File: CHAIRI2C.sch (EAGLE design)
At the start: 20 parts, among them IC1 DS3502, IC2 DS3502, X1 OUTPUT

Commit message: Changed VREF on digital pots for v1.0 release
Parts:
- added U$8, U$9: FIDUCIAL1X2.5, SuperHouse-Symbols:FIDUCIAL1X2.5
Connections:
- net 12V: now also IC1.VBIAS, IC2.VBIAS
- net N$2: no longer IC1.VBIAS
- net N$3: no longer IC2.VBIAS
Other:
- note added: "(C)2020 SuperHouse Automation: www.superhouse.tv"
- note added: "Direction Control (X Axis)"
- note added: "Power Indicators"
- note added: "Speed Control (Y Axis)"
- note removed: "(C)2018-2020 SuperHouse Automation: www.superhouse.tv"
- note removed: "Direction Control"
- note removed: "Power / Status"
- note removed: "Speed Control"
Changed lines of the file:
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@@
 <part name="U$2" library="SuperHouse-Jumpers" library_urn="urn:adsk.eagle:library:12190622" deviceset="SJC" device="-NORMAL" package3d_urn="urn:adsk.eagle:package:7066342/1" value="PU"/>
 <part name="U$3" library="SuperHouse-Jumpers" library_urn="urn:adsk.eagle:library:12190622" deviceset="SJC" device="-NORMAL" package3d_urn="urn:adsk.eagle:package:7066342/1" value="PU"/>
+<part name="U$8" library="SuperHouse-Symbols" library_urn="urn:adsk.eagle:library:13228893" deviceset="FIDUCIAL" device="1X2.5" package3d_urn="urn:adsk.eagle:package:13228898/1"/>
+<part name="U$9" library="SuperHouse-Symbols" library_urn="urn:adsk.eagle:library:13228893" deviceset="FIDUCIAL" device="1X2.5" package3d_urn="urn:adsk.eagle:package:13228898/1"/>
 </parts>
 <sheets>
@@
 <text x="172.72" y="14.478" size="1.778" layer="94">V1.0 (2020-05-05)</text>
 <text x="142.24" y="14.478" size="1.778" layer="94">SKU: CHAIRI2C</text>
-<text x="141.986" y="9.398" size="1.778" layer="94">(C)2018-2020 SuperHouse Automation: www.superhouse.tv</text>
+<text x="141.986" y="9.398" size="1.778" layer="94">(C)2020 SuperHouse Automation: www.superhouse.tv</text>
 <text x="141.986" y="6.35" size="1.778" layer="94">Licensed under the TAPR Open Hardware License: www.tapr.org/ohl</text>
 <text x="202.946" y="14.478" size="1.778" layer="94">www.superhouse.tv/chairi2c</text>
-<text x="66.04" y="50.8" size="2.54" layer="94" ratio="12">Power / Status</text>
+<text x="66.04" y="50.8" size="2.54" layer="94" ratio="12">Power Indicators</text>
 <frame x1="139.7" y1="12.7" x2="243.84" y2="25.4" columns="0" rows="0" layer="94" border-left="no" border-top="no" border-right="no" border-bottom="no"/>
 <frame x1="139.7" y1="12.7" x2="170.18" y2="17.78" columns="8" rows="5" layer="94"/>
 <frame x1="170.18" y1="12.7" x2="200.66" y2="17.78" columns="8" rows="5" layer="94"/>
 <frame x1="139.7" y1="5.08" x2="243.84" y2="17.78" columns="0" rows="0" layer="94" border-left="no" border-top="no" border-right="no" border-bottom="no"/>
-<text x="71.12" y="106.68" size="2.54" layer="94" ratio="12">Direction Control</text>
-<text x="71.12" y="162.56" size="2.54" layer="94" ratio="12">Speed Control</text>
+<text x="71.12" y="106.68" size="2.54" layer="94" ratio="12">Direction Control (X Axis)</text>
+<text x="71.12" y="162.56" size="2.54" layer="94" ratio="12">Speed Control (Y Axis)</text>
 <text x="167.64" y="139.7" size="2.54" layer="94" ratio="12">Chair Interface</text>
 <wire x1="129.54" y1="119.38" x2="129.54" y2="167.64" width="0.3048" layer="97" style="longdash"/>
@@
 <attribute name="VALUE" x="49.53" y="124.46" size="1.778" layer="96" rot="R90"/>
 </instance>
+<instance part="U$8" gate="G$1" x="238.76" y="27.94" smashed="yes"/>
+<instance part="U$9" gate="G$1" x="233.68" y="27.94" smashed="yes"/>
 </instances>
 <busses>
@@
 <segment>
 <pinref part="IC1" gate="G$1" pin="RW"/>
-<wire x1="109.22" y1="142.24" x2="149.86" y2="142.24" width="0.1524" layer="91"/>
+<wire x1="109.22" y1="142.24" x2="137.16" y2="142.24" width="0.1524" layer="91"/>
 <pinref part="X1" gate="G$1" pin="1"/>
-<label x="149.86" y="116.84" size="1.27" layer="95" rot="R180" xref="yes"/>
-<wire x1="149.86" y1="116.84" x2="198.12" y2="116.84" width="0.1524" layer="91"/>
-<wire x1="149.86" y1="142.24" x2="149.86" y2="116.84" width="0.1524" layer="91"/>
-<junction x="149.86" y="116.84"/>
+<wire x1="137.16" y1="116.84" x2="198.12" y2="116.84" width="0.1524" layer="91"/>
+<wire x1="137.16" y1="142.24" x2="137.16" y2="116.84" width="0.1524" layer="91"/>
+<label x="167.64" y="116.84" size="1.778" layer="95"/>
 </segment>
 </net>
@@
 <segment>
 <pinref part="X1" gate="G$1" pin="2"/>
-<label x="149.86" y="114.3" size="1.27" layer="95" rot="R180" xref="yes"/>
 <pinref part="IC2" gate="G$1" pin="RW"/>
-<wire x1="149.86" y1="114.3" x2="198.12" y2="114.3" width="0.1524" layer="91"/>
-<wire x1="109.22" y1="86.36" x2="149.86" y2="86.36" width="0.1524" layer="91"/>
-<wire x1="149.86" y1="114.3" x2="149.86" y2="86.36" width="0.1524" layer="91"/>
-<junction x="149.86" y="114.3"/>
+<wire x1="137.16" y1="114.3" x2="198.12" y2="114.3" width="0.1524" layer="91"/>
+<wire x1="109.22" y1="86.36" x2="137.16" y2="86.36" width="0.1524" layer="91"/>
+<wire x1="137.16" y1="114.3" x2="137.16" y2="86.36" width="0.1524" layer="91"/>
+<label x="167.64" y="114.3" size="1.778" layer="95"/>
 </segment>
 </net>
@@
 <wire x1="116.84" y1="157.48" x2="116.84" y2="160.02" width="0.1524" layer="91"/>
 <pinref part="U$4" gate="G$1" pin="12V"/>
+<pinref part="IC1" gate="G$1" pin="VBIAS"/>
+<wire x1="109.22" y1="147.32" x2="111.76" y2="147.32" width="0.1524" layer="91"/>
+<wire x1="111.76" y1="147.32" x2="111.76" y2="160.02" width="0.1524" layer="91"/>
+<wire x1="111.76" y1="160.02" x2="116.84" y2="160.02" width="0.1524" layer="91"/>
+<junction x="116.84" y="160.02"/>
 </segment>
 <segment>
@@
 <wire x1="116.84" y1="101.6" x2="116.84" y2="104.14" width="0.1524" layer="91"/>
 <pinref part="U$6" gate="G$1" pin="12V"/>
+<pinref part="IC2" gate="G$1" pin="VBIAS"/>
+<wire x1="109.22" y1="91.44" x2="111.76" y2="91.44" width="0.1524" layer="91"/>
+<wire x1="111.76" y1="91.44" x2="111.76" y2="104.14" width="0.1524" layer="91"/>
+<wire x1="111.76" y1="104.14" x2="116.84" y2="104.14" width="0.1524" layer="91"/>
+<junction x="116.84" y="104.14"/>
 </segment>
 <segment>
@@
 <net name="N$2" class="0">
 <segment>
-<pinref part="IC1" gate="G$1" pin="VBIAS"/>
-<wire x1="109.22" y1="147.32" x2="111.76" y2="147.32" width="0.1524" layer="91"/>
-<wire x1="111.76" y1="147.32" x2="111.76" y2="144.78" width="0.1524" layer="91"/>
 <pinref part="IC1" gate="G$1" pin="RH"/>
-<wire x1="111.76" y1="144.78" x2="109.22" y2="144.78" width="0.1524" layer="91"/>
-<junction x="111.76" y="144.78"/>
-<wire x1="111.76" y1="144.78" x2="116.84" y2="144.78" width="0.1524" layer="91"/>
+<wire x1="109.22" y1="144.78" x2="116.84" y2="144.78" width="0.1524" layer="91"/>
 <pinref part="R2" gate="G$1" pin="1"/>
 <wire x1="116.84" y1="144.78" x2="116.84" y2="147.32" width="0.1524" layer="91"/>
@@
 <net name="N$3" class="0">
 <segment>
-<pinref part="IC2" gate="G$1" pin="VBIAS"/>
-<wire x1="109.22" y1="91.44" x2="111.76" y2="91.44" width="0.1524" layer="91"/>
-<wire x1="111.76" y1="91.44" x2="111.76" y2="88.9" width="0.1524" layer="91"/>
 <pinref part="IC2" gate="G$1" pin="RH"/>
-<wire x1="111.76" y1="88.9" x2="109.22" y2="88.9" width="0.1524" layer="91"/>
-<wire x1="111.76" y1="88.9" x2="116.84" y2="88.9" width="0.1524" layer="91"/>
-<junction x="111.76" y="88.9"/>
+<wire x1="109.22" y1="88.9" x2="116.84" y2="88.9" width="0.1524" layer="91"/>
 <pinref part="R3" gate="G$1" pin="1"/>
 <wire x1="116.84" y1="88.9" x2="116.84" y2="91.44" width="0.1524" layer="91"/>
@@
 </sheet>
 </sheets>
-<errors>
-</errors>
 </schematic>
 </drawing>

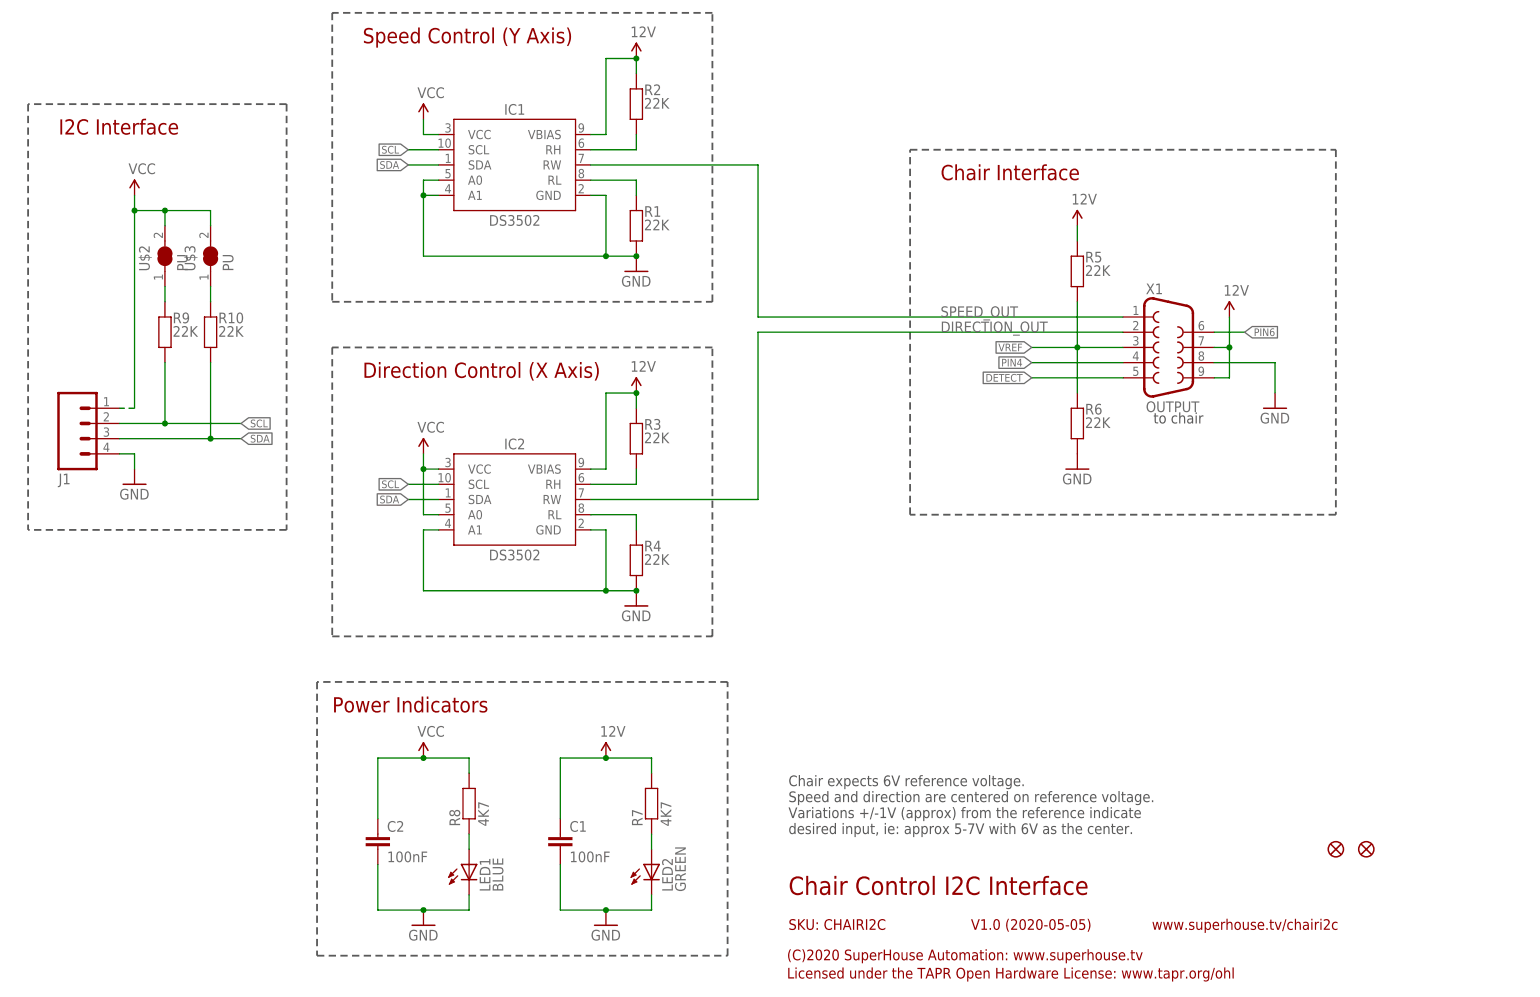
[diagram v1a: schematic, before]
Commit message: Changed reference bias and exposed extra connections
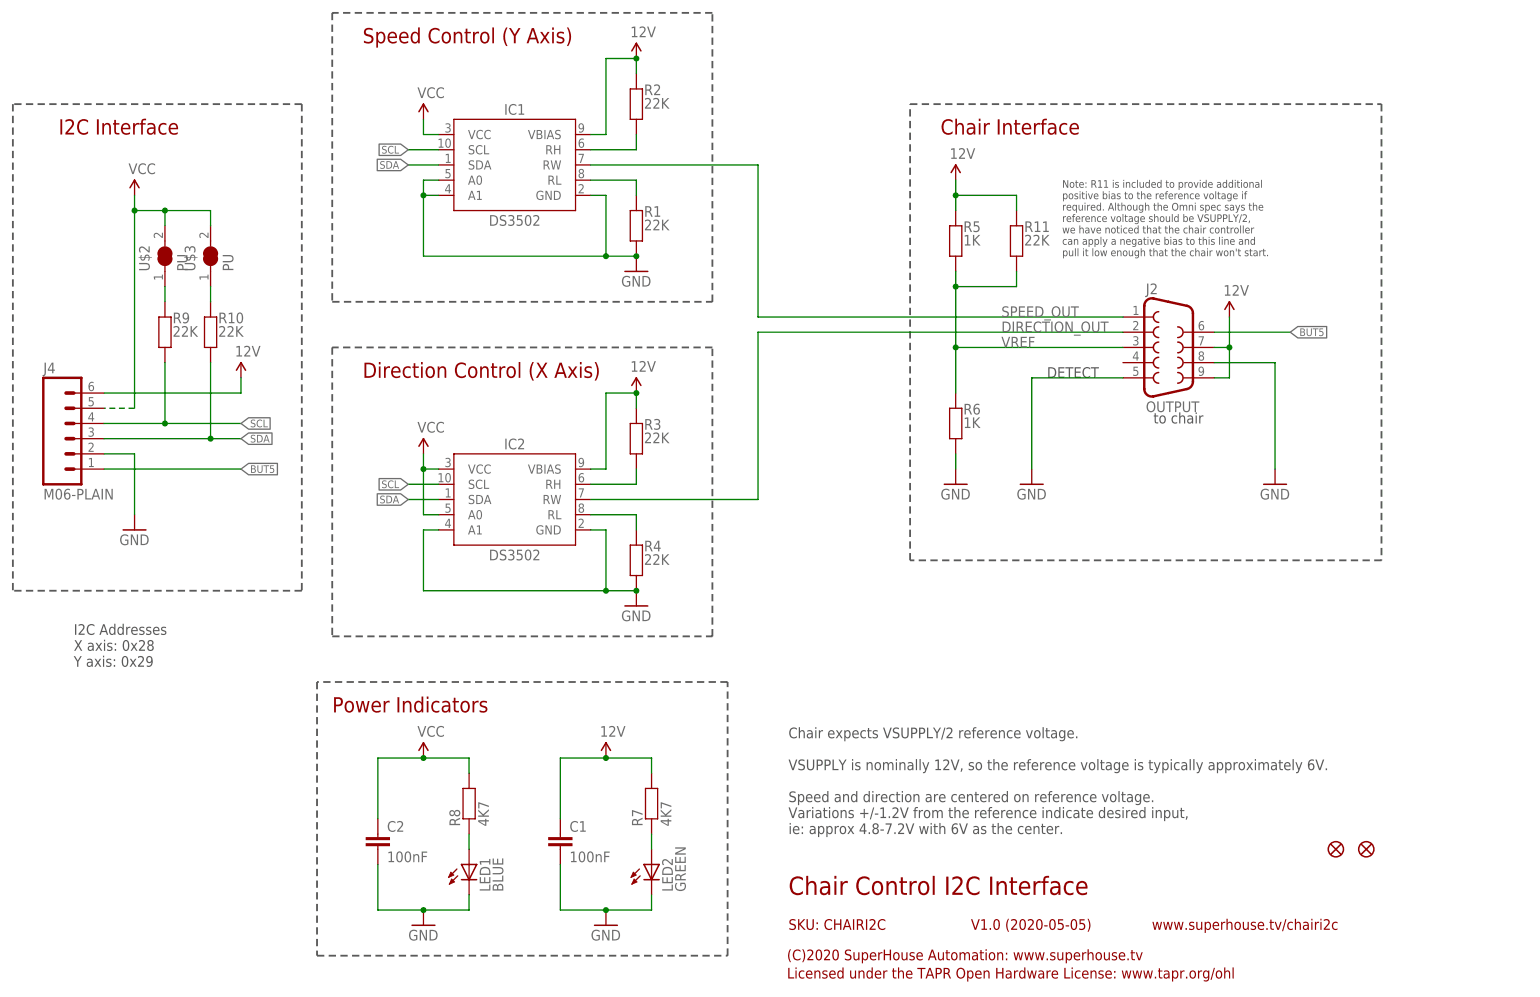
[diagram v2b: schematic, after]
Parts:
- removed J1: (no value), SuperHouse-Connectors:M04-PLAIN
- added J4: M06-PLAIN, SuperHouse-Connectors:M06-PLAIN
- added R11: 22K, SuperHouse-DiscreteSemi:RESISTOR0603
- R5, R6: value 22K -> 1K
- renumbered X1 to J2
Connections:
- removed net DETECT: J2.5
- removed net PIN4: J2.4
- removed net PIN6: J2.6
- new net BUT5: J2.6, J4.1
- net 12V: now also J4.6, R11.2
- net GND: now also J2.5, J4.2; no longer J1.4
- net SCL: now also J4.4; no longer J1.2
- net SDA: now also J4.3; no longer J1.3
- net VCC: now also J4.5; no longer J1.1
- net VREF: now also R11.1
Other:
- note added: "Chair expects VSUPPLY/2 reference voltage. VSUPPLY is nominally 12V, so the reference voltage is typically approximately 6V. Speed and direction are centered on reference voltage. Variations +/-1.2V from the reference indicate desired input, ie: approx 4.8-7.2V with 6V as the center."
- note added: "DETECT"
- note added: "I2C Addresses X axis: 0x28 Y axis: 0x29"
- note added: "Note: R11 is included to provide additional positive bias to the reference voltage if required. Although the Omni spec says the reference voltage should be VSUPPLY/2, we have noticed that the chair controller can apply a negative bias to this line and pull it low enough that the chair won't start."
- note removed: "Chair expects 6V reference voltage. Speed and direction are centered on reference voltage. Variations +/-1V (approx) from the reference indicate desired input, ie: approx 5-7V with 6V as the center."
- moved on the sheet: R5, R6
